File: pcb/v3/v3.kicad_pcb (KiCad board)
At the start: 2 copper layers, 100 x 100 mm, 49 parts, among them J1 RJ10, J10 USB_A, J2 ICSP, J3 RJ10, J4 RJ10, J5 RJ10, J6 RJ10, J7 RJ10, J8 BOOST, J9 USB_B, Q2 2N3904, Q3 BS170, SW1 CTL1, SW2 CTL2, SW3 CTL3, U1 ATmega328P-PU, U2 PCF8574, U3 RC1602A, Y1 16MHz

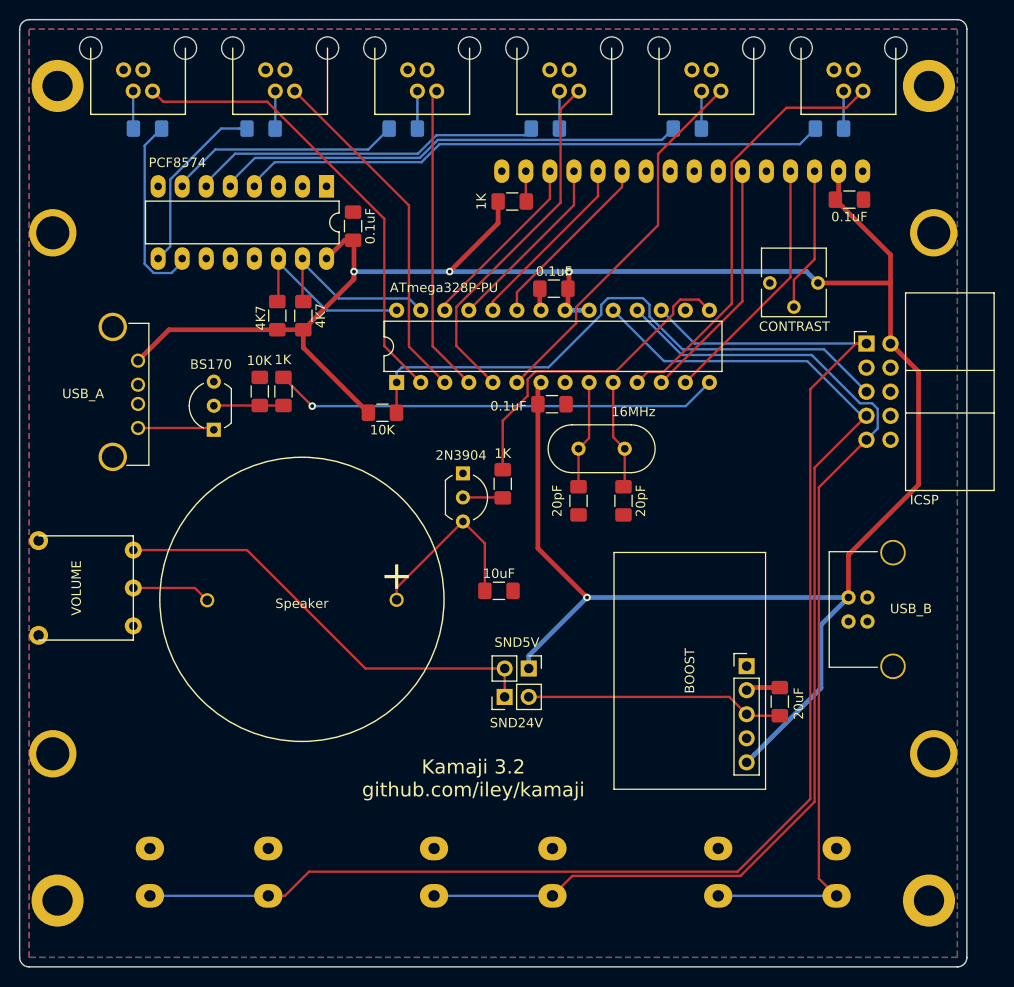
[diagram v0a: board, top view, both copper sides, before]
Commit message: Migrate v3 PCB to newer KiCAD
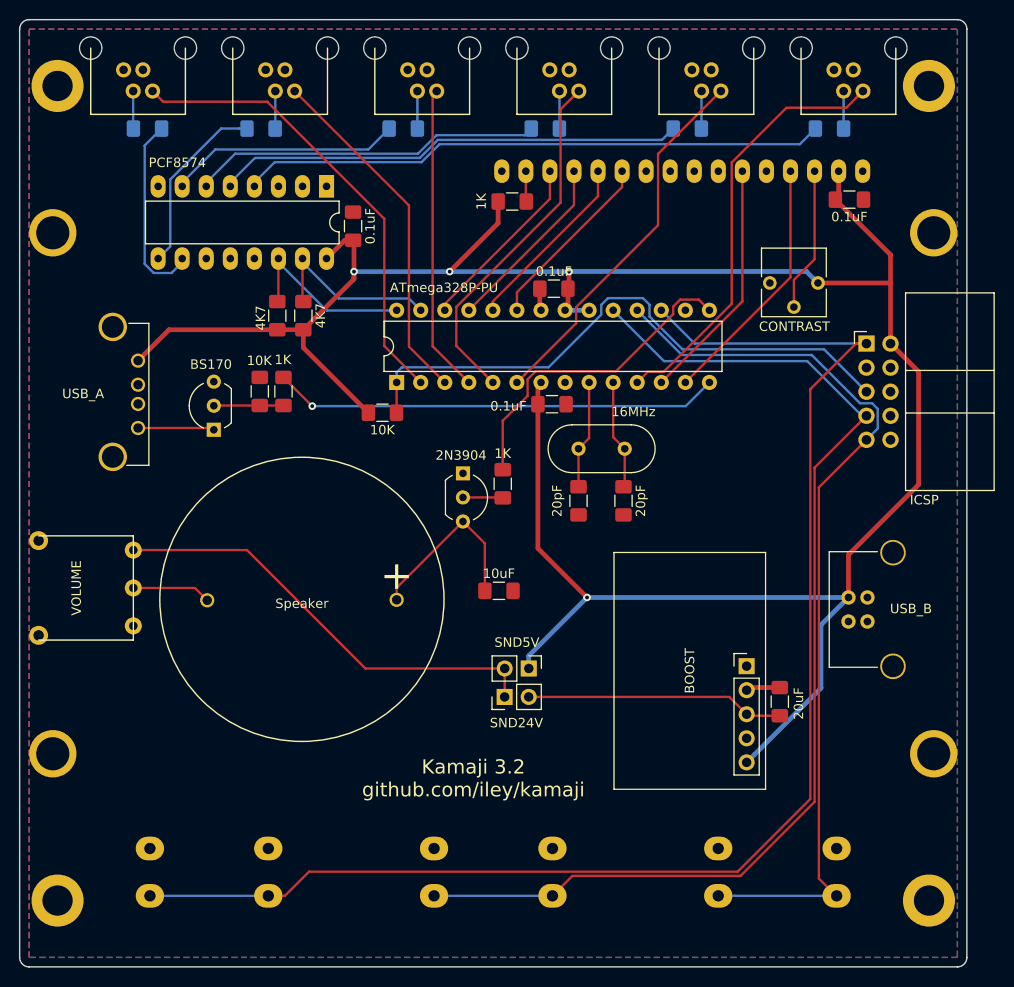
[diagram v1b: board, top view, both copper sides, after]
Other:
- net class Default removed
- net class Power removed
